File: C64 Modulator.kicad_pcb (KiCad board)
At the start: 2 copper layers, 63.5 x 63.4 mm, 35 parts, among them J1 8765, J2 4321, J3 AUD_RIGHT, J4 TRS_3.5mm, J5 RCA_PLUG, Q1 BC549, Q2 BC549, Q3 BC549, Q4 BC549, U1 LM7805

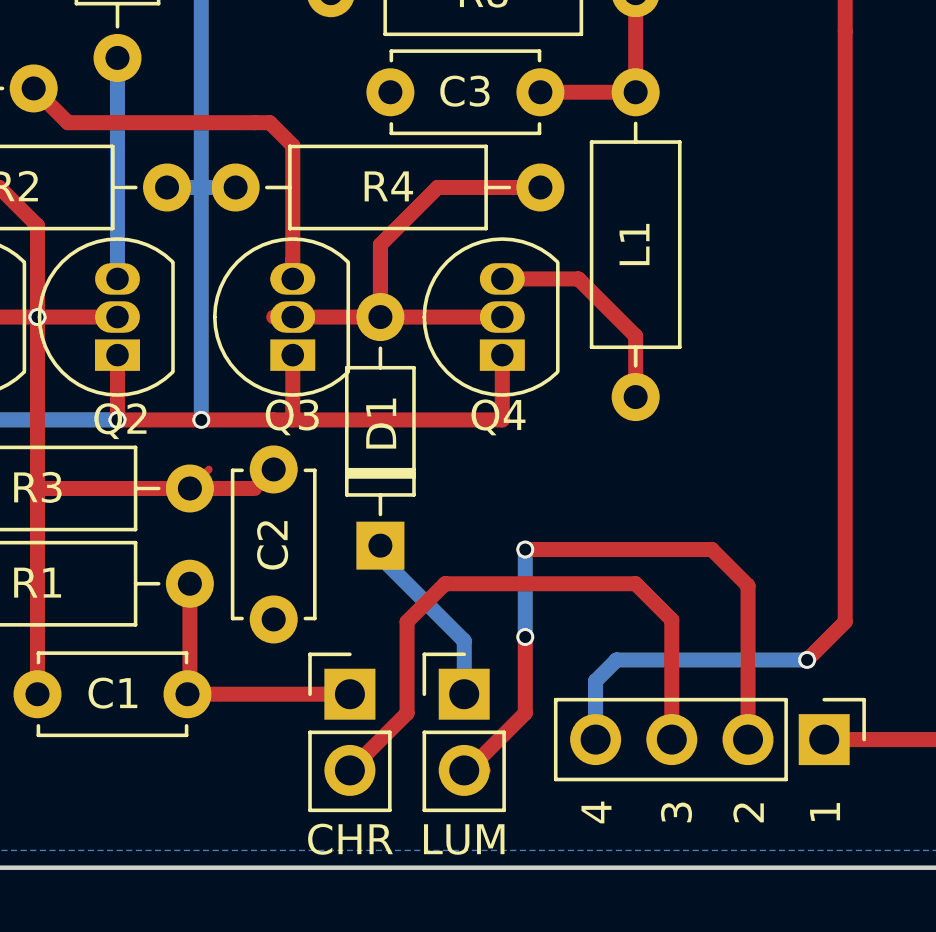
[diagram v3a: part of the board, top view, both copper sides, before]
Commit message: Clean up courtyards so they don't overlap.
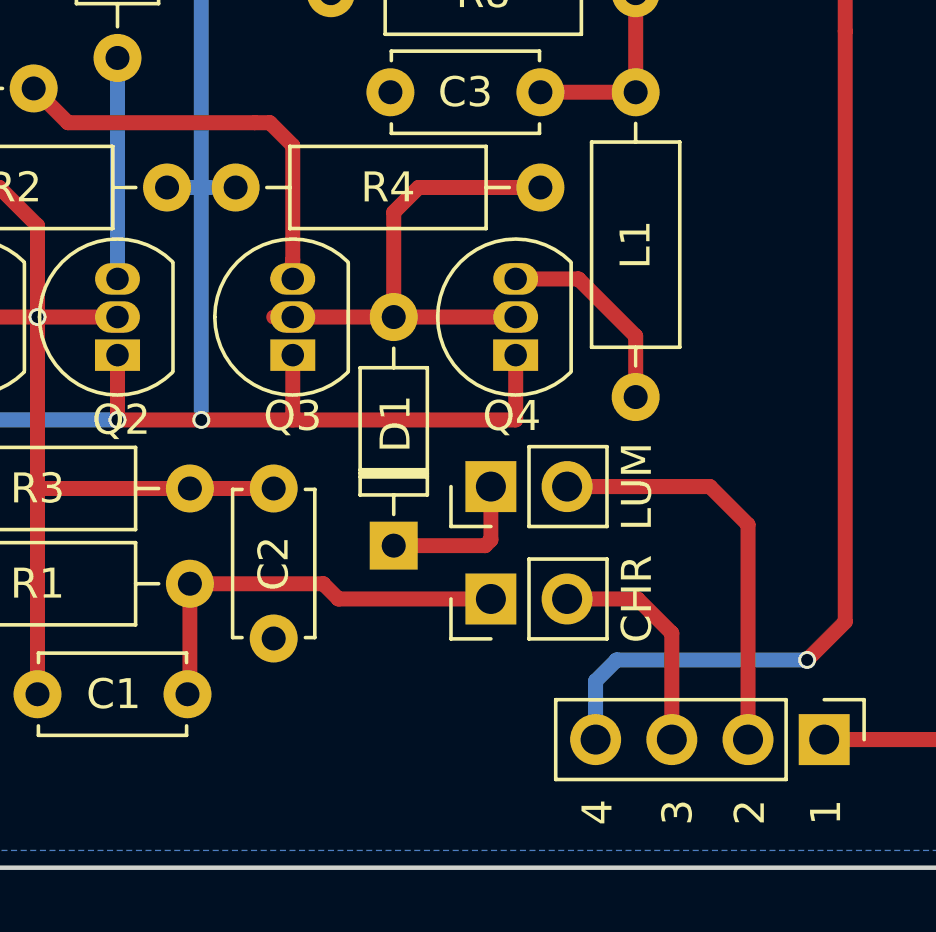
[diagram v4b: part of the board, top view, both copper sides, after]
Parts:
- moved JP2 6.98 mm to (159.0, 113.0), turned to 90 degrees
- moved JP1 5.67 mm to (159.0, 116.7), turned to 90 degrees
- moved C2 0.64 mm to (151.8, 113.0)
- moved D1 0.44 mm to (155.8, 114.9)
- moved Q4 0.44 mm to (159.8, 108.6)
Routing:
- net Net-(J2-Pad3): track 19.7 -> 7.60 mm
- net Net-(J2-Pad2): track 22.9 -> 13.7 mm, vias 2 -> 0
- net CHROMA_IN: track 9.13 -> 14.0 mm
- net Net-(C1-Pad1): track 36.0 -> 35.1 mm
- net LUMA_IN: track 6.11 -> 5.48 mm

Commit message: Re-Add mounting point supports to main board (ground pins)
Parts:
- added J3: Conn_01x01_Female, Connector_PinHeader_2.54mm:PinHeader_1x01_P2.54mm_Vertical, F.Cu at (180.9, 79.4)
- added J4: Conn_01x01_Female, Connector_PinHeader_2.54mm:PinHeader_1x01_P2.54mm_Vertical, F.Cu at (180.9, 108.9)
- added J5: Conn_01x01_Female, Connector_PinHeader_2.54mm:PinHeader_1x01_P2.54mm_Vertical, F.Cu at (120.1, 79.4)
- added J6: Conn_01x01_Female, Connector_PinHeader_2.54mm:PinHeader_1x01_P2.54mm_Vertical, F.Cu at (120.1, 108.9)
- moved C6 1.21 mm to (177.2, 78.7)
- moved C7 0.63 mm to (172.7, 80.0)
- moved C1 0.45 mm to (144.0, 119.4)
- moved U1 0.25 mm to (178.4, 89.2)
- renumbered J3 to J7, J4 to J8, J5 to J9, R9 to R8, R8 to R9
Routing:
- net VCC: track 58.2 -> 60.4 mm
- net Net-(C6-Pad1): track 31.0 -> 32.6 mm

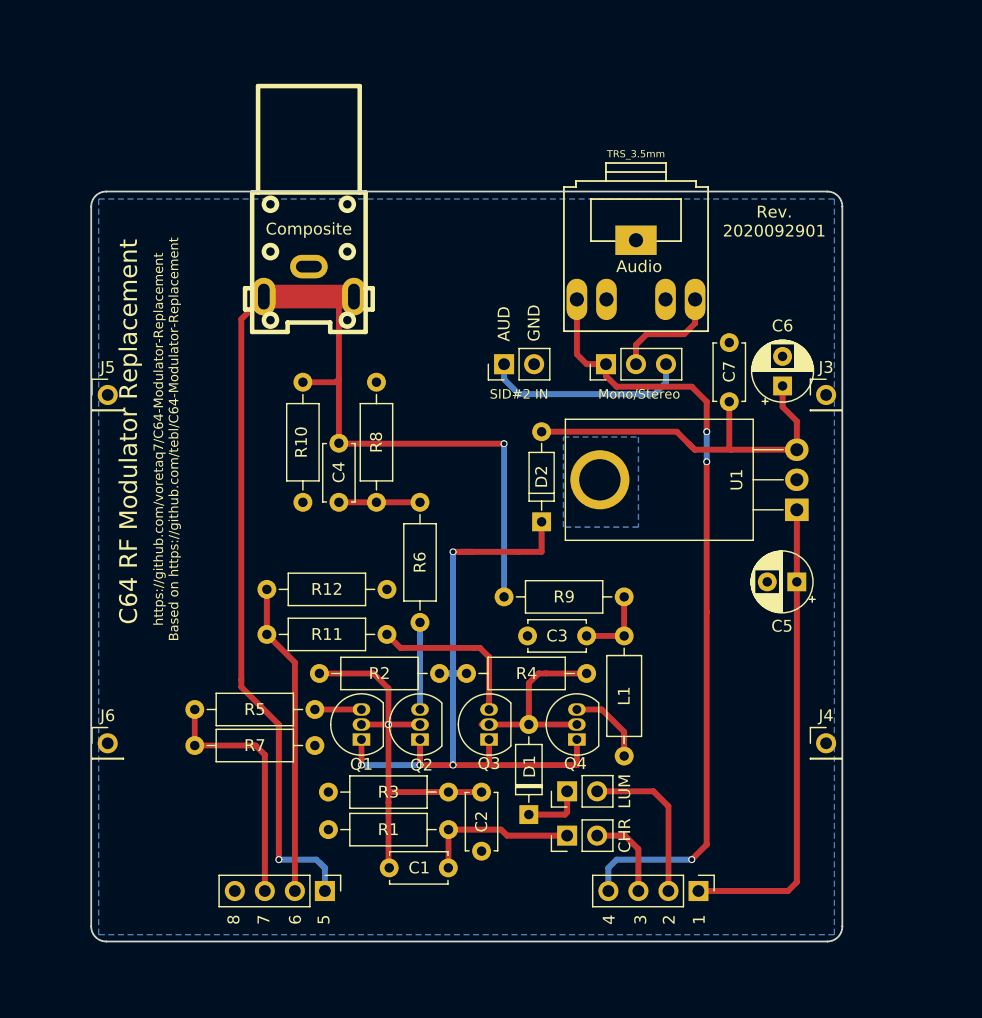
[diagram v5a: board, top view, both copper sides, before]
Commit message: Add mounting supports under RCA & TRS jack.
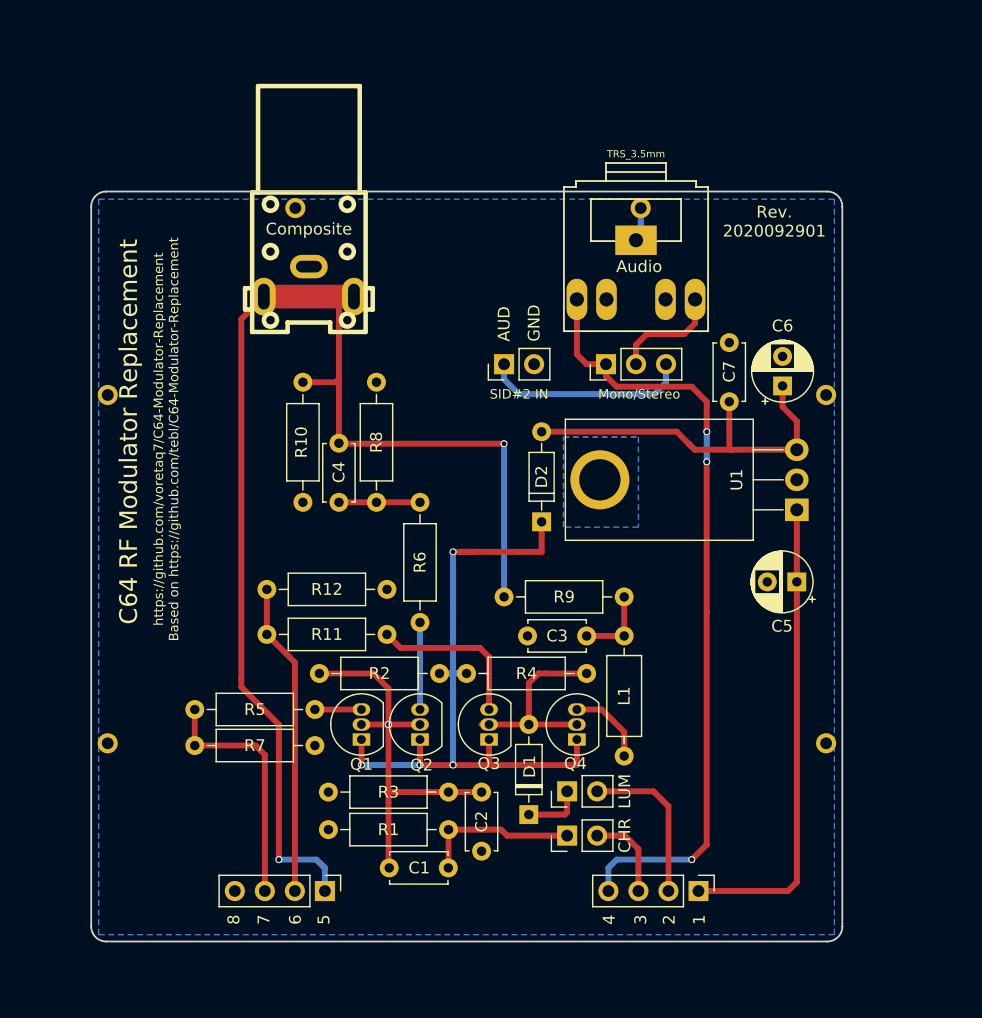
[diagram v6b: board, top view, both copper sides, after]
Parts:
- added J10: Conn_01x01_Female, Connector_PinHeader_2.54mm:PinHeader_1x01_P2.54mm_Vertical, F.Cu at (136.0, 63.6)
- added J11: Conn_01x01_Female, Connector_PinHeader_2.54mm:PinHeader_1x01_P2.54mm_Vertical, F.Cu at (165.2, 63.6)
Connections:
- U1 pad : GND -> (no net)
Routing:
- net GND: track 0.00 -> 2.89 mm
